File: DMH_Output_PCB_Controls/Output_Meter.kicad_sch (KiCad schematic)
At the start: 63 parts, among them Q1 BC558, Q2 BC558, U1 TL072, U2 LM339, U3 LM339, U4 LM339, U5 LM339, U6 LM339

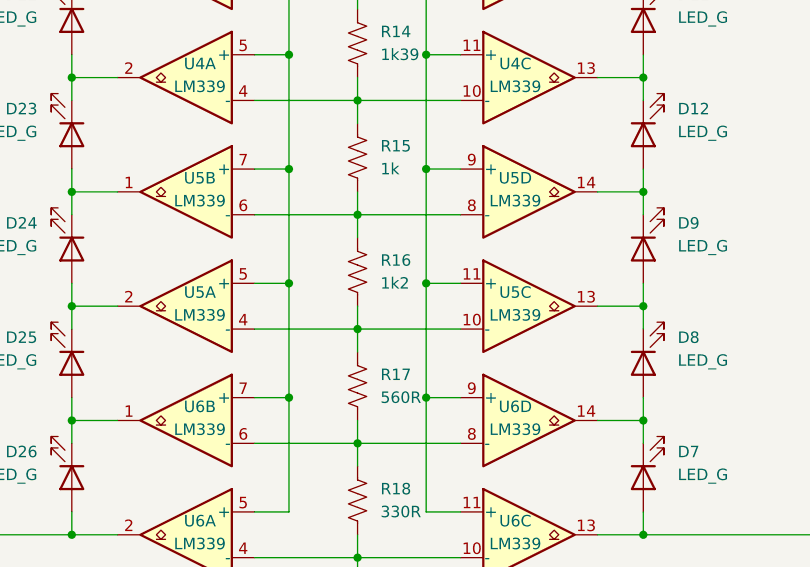
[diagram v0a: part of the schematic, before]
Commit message: Simulated 10V ref for VU meter
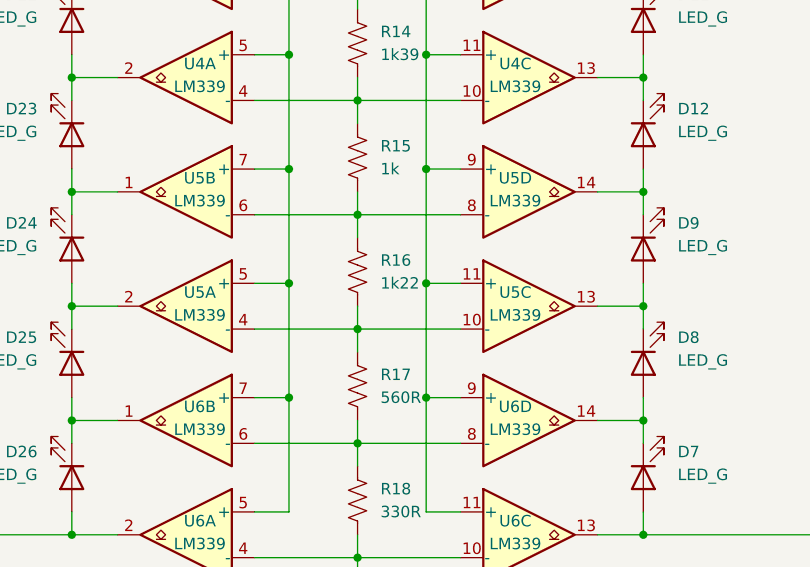
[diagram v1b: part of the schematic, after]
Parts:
- R16: value 1k2 -> 1k22
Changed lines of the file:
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@@
 			)
 		)
-		(property "Value" "1k2"
+		(property "Value" "1k22"
 			(at 173.99 124.4599 0)
 			(effects

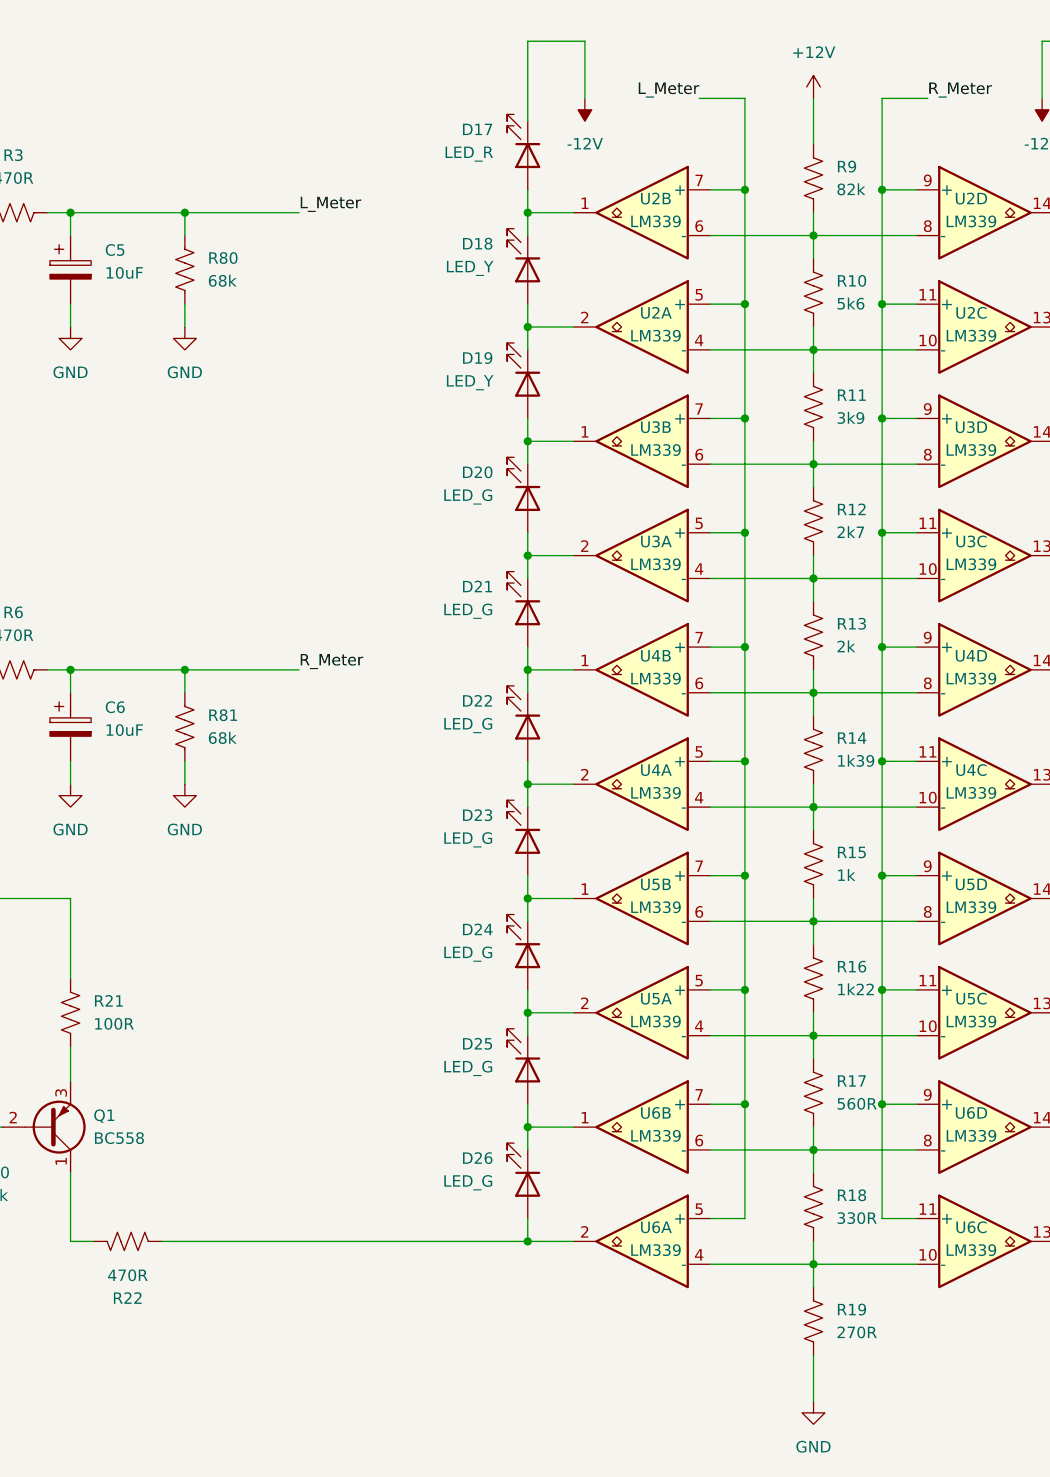
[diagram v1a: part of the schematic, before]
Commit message: Adjusted meter circuits
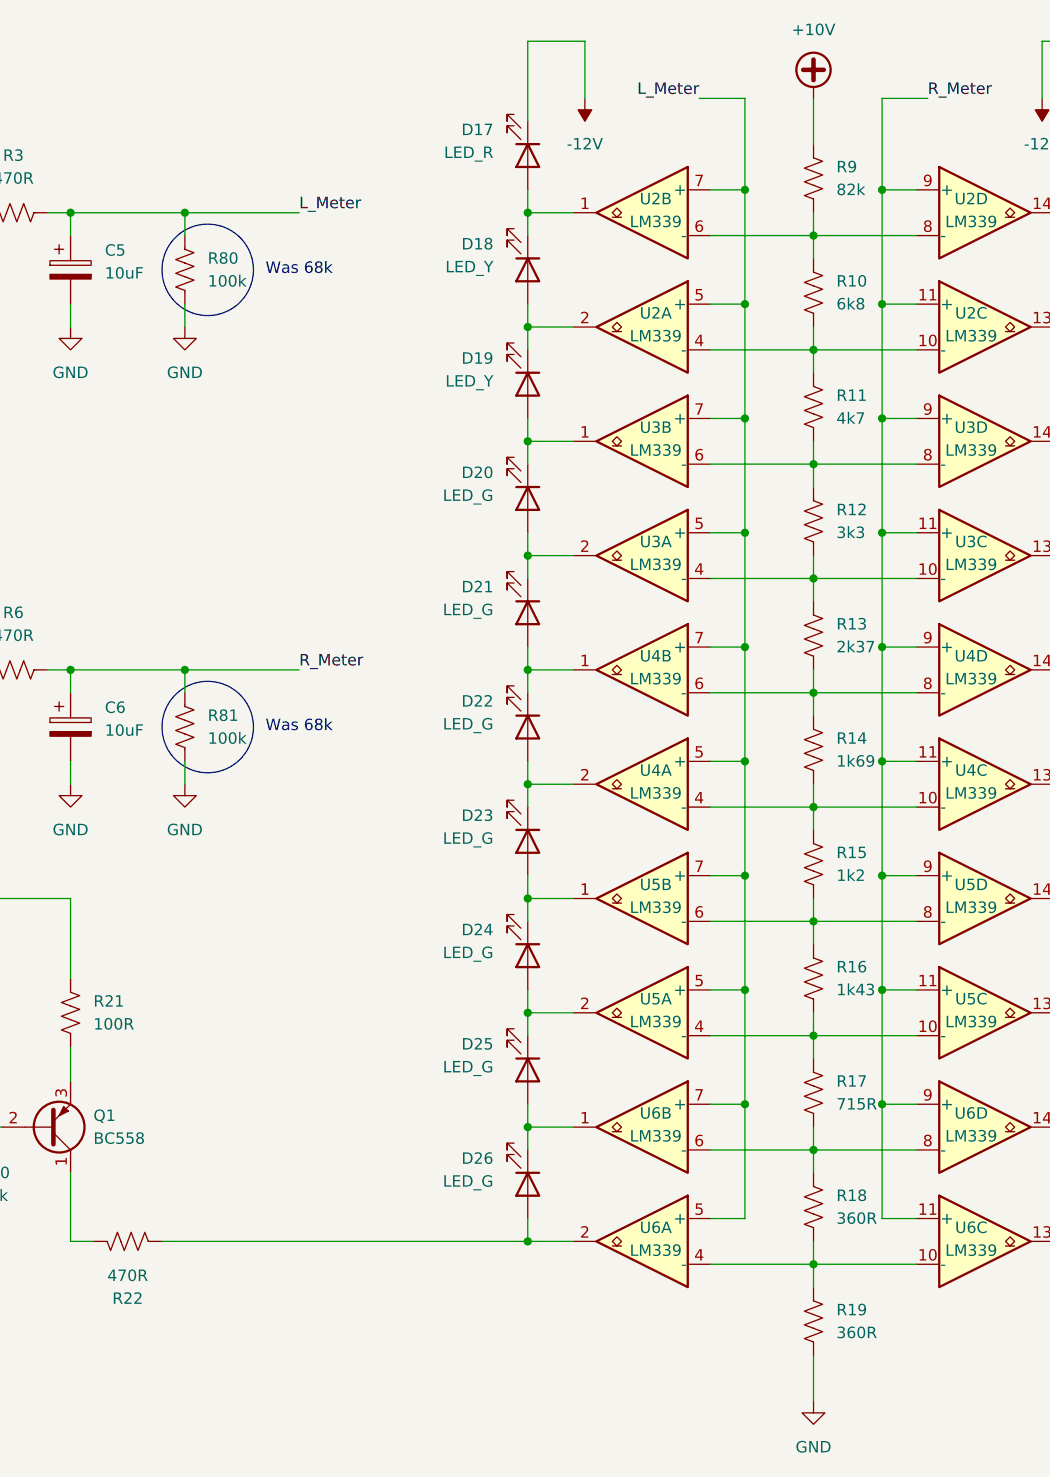
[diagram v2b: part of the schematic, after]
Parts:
- R10: value 5k6 -> 6k8
- R11: value 3k9 -> 4k7
- R12: value 2k7 -> 3k3
- R13: value 2k -> 2k37
- R14: value 1k39 -> 1k69
- R15: value 1k -> 1k2
- R16: value 1k22 -> 1k43
- R17: value 560R -> 715R
- R18: value 330R -> 360R
- R19: value 270R -> 360R
- R80, R81: value 68k -> 100k
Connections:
- net +12V: no longer R9.2
- new net +10V: R9.2
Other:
- note added: "Was 68k"
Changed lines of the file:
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@@
 		(comment 1 "PCB for 5 cm Kosmo format synthesizer module")
 	)
+	(circle
+		(center 104.14 95.25)
+		(radius 5.08)
+		(stroke
+			(width 0)
+			(type default)
+		)
+		(fill
+			(type none)
+		)
+	)
+	(circle
+		(center 104.14 44.45)
+		(radius 5.08)
+		(stroke
+			(width 0)
+			(type default)
+		)
+		(fill
+			(type none)
+		)
+	)
+	(text "Was 68k"
+		(exclude_from_sim no)
+		(at 114.3 44.45 0)
+		(effects
+			(font
+				(size 1.27 1.27)
+			)
+		)
+	)
+	(text "Was 68k"
+		(exclude_from_sim no)
+		(at 114.3 95.25 0)
+		(effects
+			(font
+				(size 1.27 1.27)
+			)
+		)
+	)
 	(junction
 		(at 139.7 139.7)
@@
 			)
 		)
-		(property "Value" "68k"
+		(property "Value" "100k"
 			(at 104.14 45.7199 0)
 			(effects
@@
 			)
 		)
-		(property "Value" "3k9"
+		(property "Value" "4k7"
 			(at 173.99 60.9599 0)
 			(effects
@@
 			)
 		)
-		(property "Value" "68k"
+		(property "Value" "100k"
 			(at 104.14 96.5199 0)
 			(effects
@@
 	)
 	(symbol
+		(lib_id "power:+VDC")
+		(at 171.45 25.4 0)
+		(unit 1)
+		(exclude_from_sim no)
+		(in_bom yes)
+		(on_board yes)
+		(dnp no)
+		(fields_autoplaced yes)
+		(property "Reference" "#PWR019"
+			(at 171.45 27.94 0)
+			(effects
+				(font
+					(size 1.27 1.27)
+				)
+				(hide yes)
+			)
+		)
+		(property "Value" "+10V"
+			(at 171.45 17.78 0)
+			(effects
+				(font
+					(size 1.27 1.27)
+				)
+			)
+		)
+		(property "Footprint" ""
+			(at 171.45 25.4 0)
+			(effects
+				(font
+					(size 1.27 1.27)
+				)
+				(hide yes)
+			)
+		)
+		(property "Datasheet" ""
+			(at 171.45 25.4 0)
+			(effects
+				(font
+					(size 1.27 1.27)
+				)
+				(hide yes)
+			)
+		)
+		(property "Description" "Power symbol creates a global label with name \"+VDC\""
+			(at 171.45 25.4 0)
+			(effects
+				(font
+					(size 1.27 1.27)
+				)
+				(hide yes)
+			)
+		)
+		(pin "1"
+		)
+		(instances
+			(project "DMH_Output_PCB_Controls"
+				(path "/58f4306d-5387-4983-bb08-41a2313fd315/91d96a83-7777-458d-a0c8-9961efcb16a5"
+					(reference "#PWR019")
+					(unit 1)
+				)
+			)
+		)
+	)
+	(symbol
 		(lib_id "Comparator:LM339")
 		(at 190.5 38.1 0)
@@
 			)
 		)
-		(property "Value" "560R"
+		(property "Value" "715R"
 			(at 173.99 137.1599 0)
 			(effects
@@
 			)
 		)
-		(property "Value" "330R"
+		(property "Value" "360R"
 			(at 173.99 149.8599 0)
 			(effects
@@
 			)
 		)
-		(property "Value" "1k"
+		(property "Value" "1k2"
 			(at 173.99 111.7599 0)
 			(effects
@@
 			)
 		)
-		(property "Value" "5k6"
+		(property "Value" "6k8"
 			(at 173.99 48.2599 0)
 			(effects
@@
 			)
 		)
-		(property "Value" "1k39"
+		(property "Value" "1k69"
 			(at 173.99 99.0599 0)
 			(effects
@@
 	)
 	(symbol
-		(lib_id "power:+12V")
-		(at 171.45 25.4 0)
-		(unit 1)
-		(exclude_from_sim no)
-		(in_bom yes)
-		(on_board yes)
-		(dnp no)
-		(fields_autoplaced yes)
-		(property "Reference" "#PWR019"
-			(at 171.45 29.21 0)
-			(effects
-				(font
-					(size 1.27 1.27)
-				)
-				(hide yes)
-			)
-		)
-		(property "Value" "+12V"
-			(at 171.45 20.32 0)
-			(effects
-				(font
-					(size 1.27 1.27)
-				)
-			)
-		)
-		(property "Footprint" ""
-			(at 171.45 25.4 0)
-			(effects
-				(font
-					(size 1.27 1.27)
-				)
-				(hide yes)
-			)
-		)
-		(property "Datasheet" ""
-			(at 171.45 25.4 0)
-			(effects
-				(font
-					(size 1.27 1.27)
-				)
-				(hide yes)
-			)
-		)
-		(property "Description" "Power symbol creates a global label with name \"+12V\""
-			(at 171.45 25.4 0)
-			(effects
-				(font
-					(size 1.27 1.27)
-				)
-				(hide yes)
-			)
-		)
-		(pin "1"
-		)
-		(instances
-			(project "DMH_Output_PCB_1"
-				(path "/58f4306d-5387-4983-bb08-41a2313fd315/91d96a83-7777-458d-a0c8-9961efcb16a5"
-					(reference "#PWR019")
-					(unit 1)
-				)
-			)
-		)
-	)
-	(symbol
 		(lib_id "Device:R_US")
 		(at 31.75 48.26 90)
@@
 			)
 		)
-		(property "Value" "2k7"
+		(property "Value" "3k3"
 			(at 173.99 73.6599 0)
 			(effects
@@
 			)
 		)
-		(property "Value" "2k"
+		(property "Value" "2k37"
 			(at 173.99 86.3599 0)
 			(effects
@@
 			)
 		)
-		(property "Value" "1k22"
+		(property "Value" "1k43"
 			(at 173.99 124.4599 0)
 			(effects
@@
 			)
 		)
-		(property "Value" "270R"
+		(property "Value" "360R"
 			(at 173.99 162.5599 0)
 			(effects

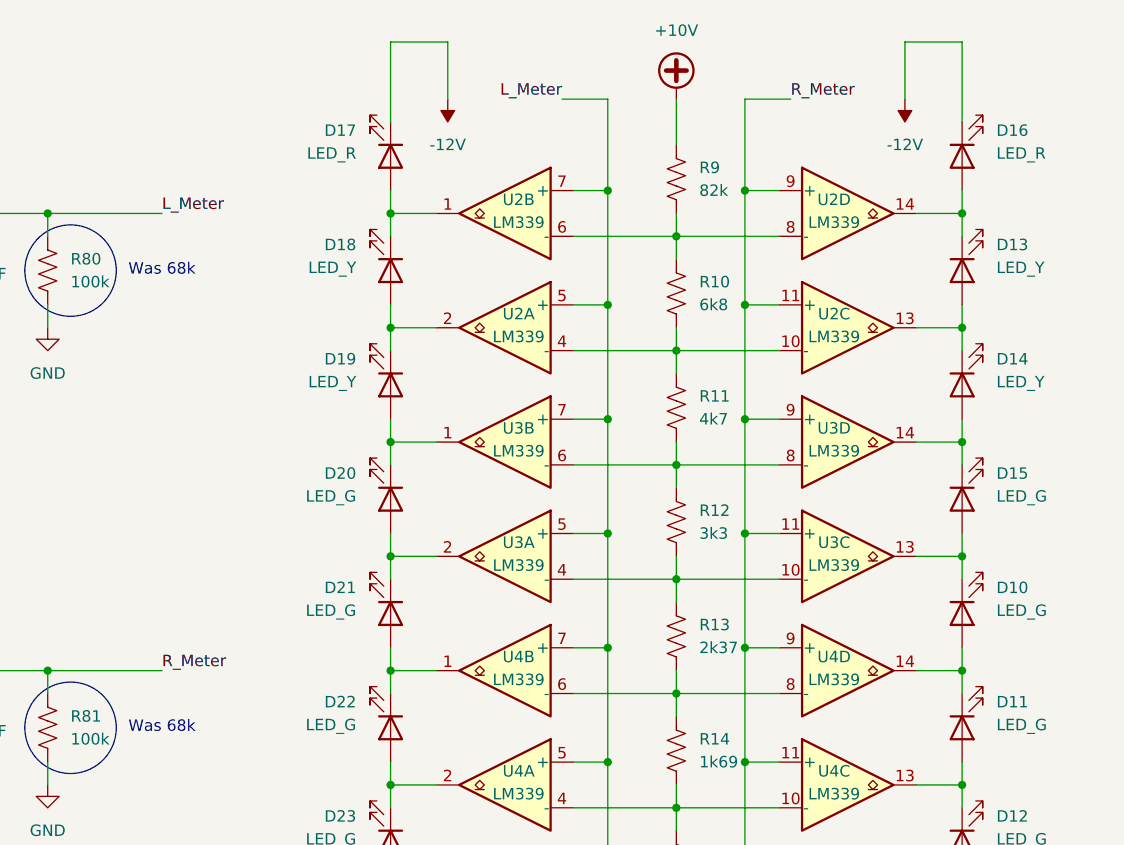
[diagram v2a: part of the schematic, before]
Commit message: Controls PCB placement ongoing
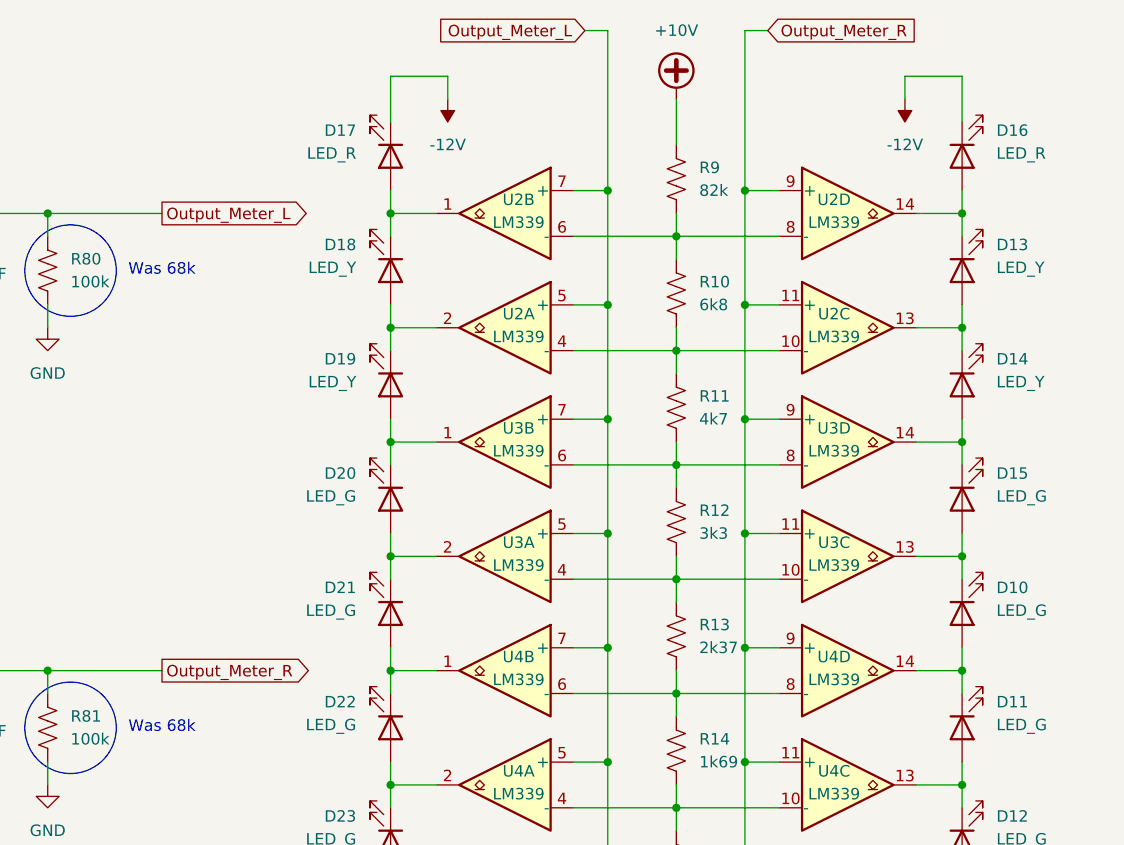
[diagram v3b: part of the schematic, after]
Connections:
- net L_Meter renamed Output_Meter_L
- net R_Meter renamed Output_Meter_R
